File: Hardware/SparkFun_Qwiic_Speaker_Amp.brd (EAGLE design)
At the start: 43.2 x 25.4 mm, 93 parts, among them J1 QWIIC, J2 TRS_INPUT, J6 SCREW, U6 TPA2016D2

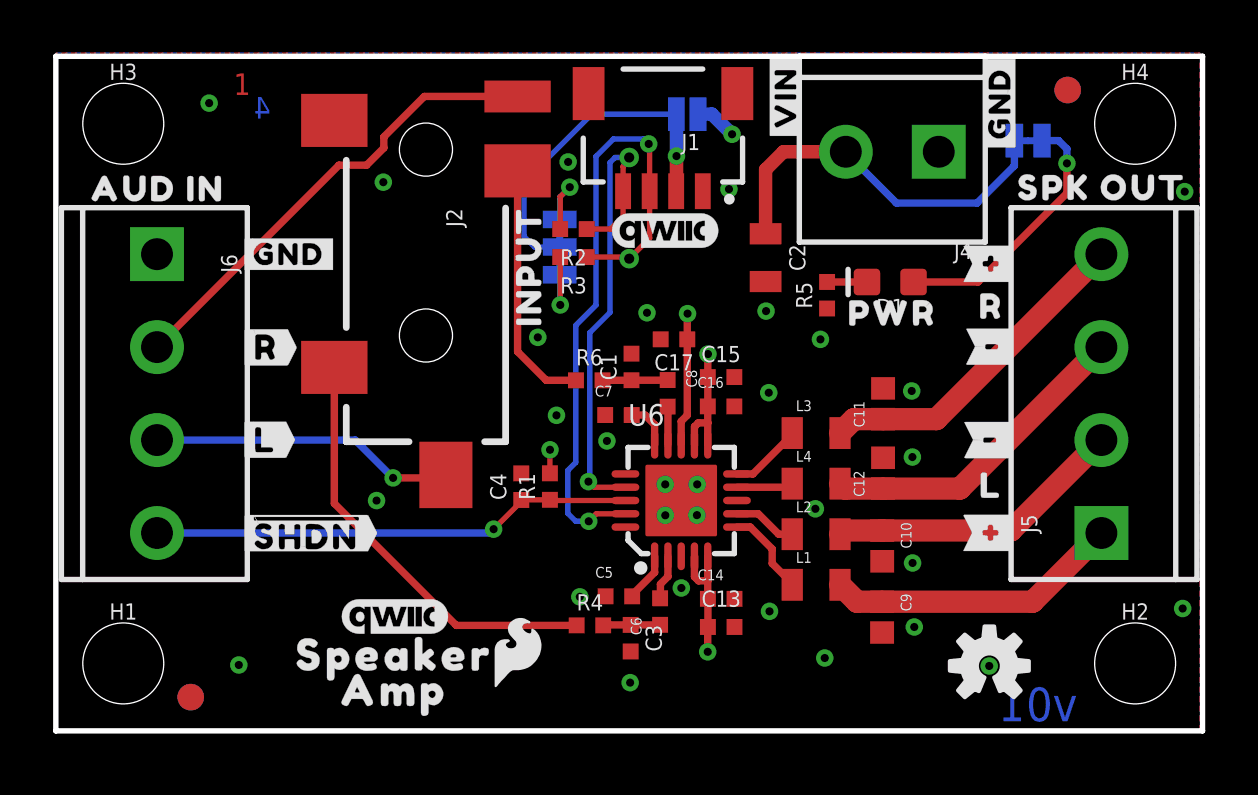
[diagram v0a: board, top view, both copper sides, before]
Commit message: Full SparkFun and flame logo on top silk
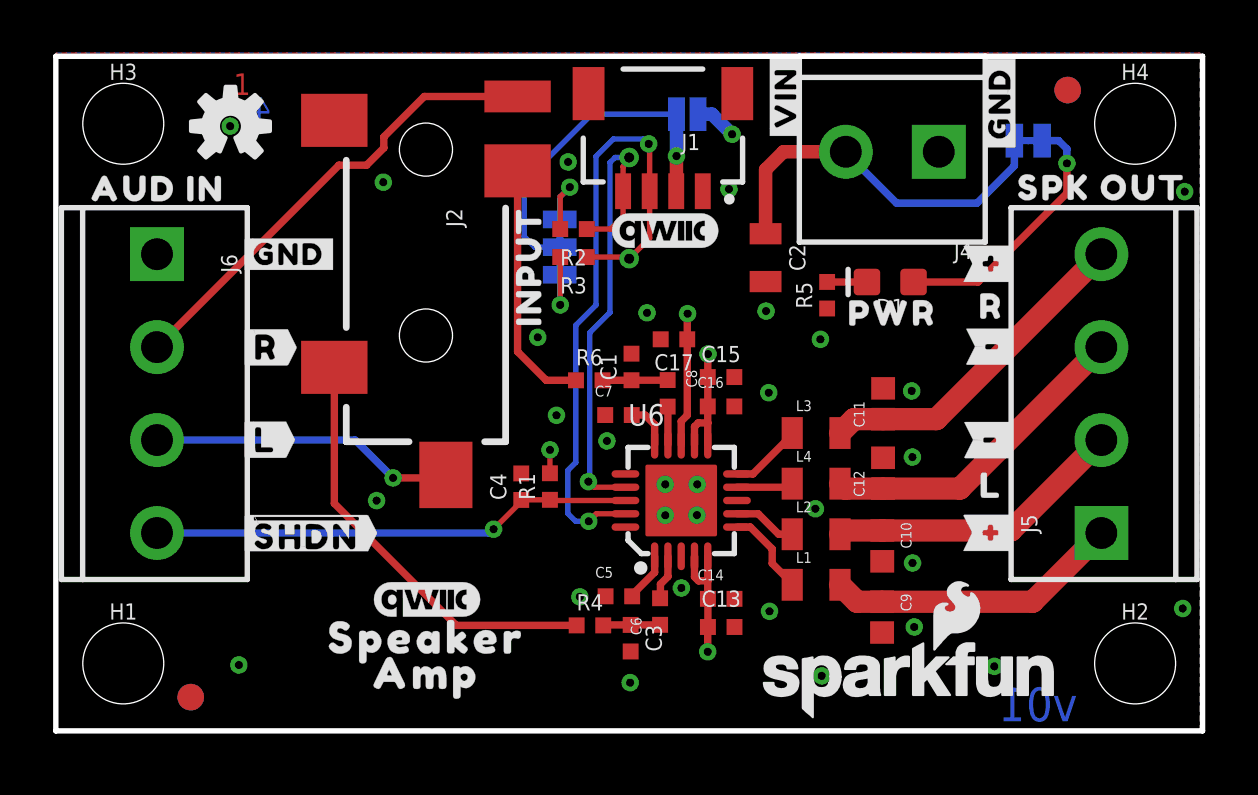
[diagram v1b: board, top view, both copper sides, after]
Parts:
- removed LOGO5: SFE_LOGO_FLAME.1_INCH, SparkFun-Aesthetics:SFE_LOGO_FLAME_.1
- added U$30: (no value), SparkFun-Aesthetics:SFE_LOGO_NAME_FLAME_.1
- moved LOGO4 35.1 mm to (6.58, 22.8)
- moved U$1 1.37 mm to (14.0, 3.50)
- moved U$6 1.37 mm to (14.0, 2.17)
- moved LOGO1 1.37 mm to (14.0, 4.94)
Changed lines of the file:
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@@
 <setting verticaltext="up"/>
 </settings>
-<grid distance="0.05" unitdist="inch" unit="inch" style="lines" multiple="1" display="yes" altdistance="0.001" altunitdist="inch" altunit="inch"/>
+<grid distance="0.05" unitdist="inch" unit="inch" style="lines" multiple="1" display="yes" altdistance="0.0001" altunitdist="inch" altunit="inch"/>
 <layers>
 <layer number="1" name="Top" color="4" fill="1" visible="yes" active="yes"/>
@@
 <layer number="98" name="Guide" color="6" fill="1" visible="no" active="no"/>
 <layer number="99" name="SpiceOrder" color="7" fill="1" visible="no" active="no"/>
-<layer number="100" name="Muster" color="7" fill="1" visible="no" active="yes"/>
+<layer number="100" name="Muster" color="7" fill="1" visible="yes" active="yes"/>
 <layer number="101" name="Patch_Top" color="12" fill="4" visible="no" active="no"/>
 <layer number="102" name="Vscore" color="7" fill="1" visible="no" active="no"/>
@@
 <element name="LOGO2" library="SparkFun-Aesthetics" package="SFE_LOGO_NAME_FLAME_.1" value="SFE_LOGO_NAME_FLAME.1_INCH" x="31.123340625" y="7.845940625" smashed="yes" rot="MR270"/>
 <element name="LOGO3" library="SparkFun-Aesthetics" package="QWIIC_4MM" value="QWIIC_LOGO_4MM" x="22.9502" y="18.8237" smashed="yes"/>
-<element name="LOGO4" library="SparkFun-Aesthetics" package="OSHW-LOGO-S" value="OSHW-LOGOS" x="35.1512625" y="2.445978125" smashed="yes"/>
+<element name="LOGO4" library="SparkFun-Aesthetics" package="OSHW-LOGO-S" value="OSHW-LOGOS" x="6.5762625" y="22.765978125" smashed="yes"/>
 <element name="FD1" library="SparkFun-Aesthetics" package="FIDUCIAL-1X2" value="FIDUCIAL1X2" x="5.08" y="1.27" smashed="yes"/>
 <element name="FD2" library="SparkFun-Aesthetics" package="FIDUCIAL-1X2" value="FIDUCIAL1X2" x="5.08" y="1.27" smashed="yes" rot="MR0"/>
@@
 <attribute name="VALUE" value="1nF" x="32.291021875" y="8.6233" size="0.4064" layer="27" rot="R90"/>
 </element>
-<element name="U$6" library="output" package="AMP0" value="" x="12.7508" y="1.524" smashed="yes"/>
+<element name="U$6" library="output" package="AMP0" value="" x="13.959840625" y="2.16661875" smashed="yes"/>
 <element name="J2" library="SparkFun-Connectors" package="AUDIO-JACK-3.5MM-SMD" value="TRS_INPUT" x="13.93698125" y="25.3873" smashed="yes" rot="R270">
 <attribute name="NAME" x="14.69898125" y="19.6723" size="0.6096" layer="25" font="vector" ratio="20" rot="R270"/>
@@
 <attribute name="VALUE" value="0.1uF" x="23.969978125" y="11.0744" size="0.4064" layer="27"/>
 </element>
-<element name="U$1" library="output" package="SPEAKER0" value="" x="12.760959375" y="2.854959375" smashed="yes"/>
+<element name="U$1" library="output" package="SPEAKER0" value="" x="13.97" y="3.497578125" smashed="yes"/>
 <element name="U$3" library="output" package="INPUT0" value="" x="17.807940625" y="17.51584375" smashed="yes" rot="R90"/>
 <element name="U$2" library="output" package="#I2C#0" value="" x="20.59431875" y="18.277840625" smashed="yes" rot="MR270"/>
-<element name="LOGO5" library="SparkFun-Aesthetics" package="SFE_LOGO_FLAME_.1" value="SFE_LOGO_FLAME.1_INCH" x="17.383765625" y="2.974340625" smashed="yes"/>
 <element name="U$4" library="output" package="SPEAKER0" value="" x="15.118084375" y="7.150103125" smashed="yes" rot="MR0"/>
 <element name="U$7" library="SparkFun-Aesthetics" package="QWIIC_5.5MM" value="" x="15.372084375" y="8.928103125" smashed="yes" rot="MR0"/>
@@
 <element name="U$10" library="output" package="###16" value="" x="35.30091875" y="14.4653" smashed="yes"/>
 <element name="U$12" library="output" package="###15" value="" x="35.265359375" y="17.58441875" smashed="yes"/>
-<element name="LOGO1" library="SparkFun-Aesthetics" package="QWIIC_4MM" value="QWIIC_LOGO_4MM" x="12.774959375" y="4.294903125" smashed="yes"/>
+<element name="LOGO1" library="SparkFun-Aesthetics" package="QWIIC_4MM" value="QWIIC_LOGO_4MM" x="13.984" y="4.937521875" smashed="yes"/>
 <element name="U$14" library="output" package="R21" value="" x="35.2272625" y="15.984221875" smashed="yes"/>
 <element name="U$21" library="output" package="SPK_OUT22" value="" x="39.410640625" y="20.449540625" smashed="yes"/>
@@
 <element name="U$40" library="output" package="##SHDN##2" value="" x="9.4361" y="7.44728125" smashed="yes"/>
 <element name="U$13" library="output" package="##SHDN##3" value="" x="6.9088" y="7.439659375" smashed="yes" rot="MR0"/>
+<element name="U$30" library="SparkFun-Aesthetics" package="SFE_LOGO_NAME_FLAME_.1" value="" x="32.184340625" y="1.932940625" smashed="yes"/>
 </elements>
 <signals>
@@
 <vertex x="43.18" y="0"/>
 </polygon>
-<via x="5.773421875" y="23.637240625" extent="1-16" drill="0.3048"/>
+<via x="6.565903125" y="22.7711" extent="1-16" drill="0.3048"/>
 <contactref element="C14" pad="2"/>
 <contactref element="U6" pad="8"/>
@@
 <via x="23.55341875" y="5.379715625" extent="1-16" drill="0.3048"/>
 <via x="28.600396875" y="8.361678125" extent="1-16" drill="0.3048"/>
-<via x="28.953459375" y="2.743196875" extent="1-16" drill="0.3048"/>
+<via x="28.83661875" y="2.070096875" extent="1-16" drill="0.3048"/>
 <via x="26.873203125" y="4.500875" extent="1-16" drill="0.3048"/>
 <via x="19.73071875" y="5.046978125" extent="1-16" drill="0.3048"/>
@@
 <via x="21.6255625" y="1.8161" extent="1-16" drill="0.3048"/>
 <via x="6.891021875" y="2.48158125" extent="1-16" drill="0.3048"/>
-<via x="35.145984375" y="2.44348125" extent="1-16" drill="0.3048"/>
+<via x="35.336484375" y="2.428240625" extent="1-16" drill="0.3048"/>
 <contactref element="C2" pad="2"/>
 <contactref element="C4" pad="2"/>
